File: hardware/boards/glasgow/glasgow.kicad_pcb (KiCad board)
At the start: 4 copper layers, 80 x 49 mm, 240 parts, among them J1 USB_B_Micro, J10 Conn_01x03, J2 Conn_02x10_Odd_Even, J3 Conn_02x10_Odd_Even, J4 Conn_01x02, J5 Conn_02x22_Odd_Even, J6 Conn_01x08, J7 Conn_01x08, J8 Conn_01x08, J9 Conn_01x08, U1 CY7C68013A-56LTX, U10 SN74LVC1T45DRL, U11 SN74LVC1T45DRL, U12 ADC081C021CIMM, U13 DAC081C081CIMK, U14 TPS73101DBV, U15 TPD3S014, U16 SN74LVC1T45DRL, U17 SN74LVC1T45DRL, U18 SN74LVC1T45DRL, U19 PCA6408APW, U2 CAT24M01W, U20 DAC081C081CIMK, U21 ADC081C021CIMM, U22 SN74LVC1T45DRL, U23 SN74LVC1T45DRL, U24 SN74LVC1T45DRL, U25 SN74LVC1T45DRL, U26 SN74LVC1T45DRL, U27 SN74LVC1T45DRL, U28 SN74LVC1T45DRL, U29 SN74LVC1T45DRL, U3 CAT24C256W, U30 ICE40HX8K-BG121, U31 TPS73101DBV, U32 SN74LVC1T45DRL, U33 MG2040, U34 ATECC508A, U35 MG2040, U36 TLV75533PDRVR, U4 SN74LVC1T45DRL, U5 PCA6408APW, U6 SN74LVC1T45DRL, U7 LM3880MF-1AF, U8 TLV73312PQDRVRQ1, U9 SN74LVC1T45DRL, Y1 24M

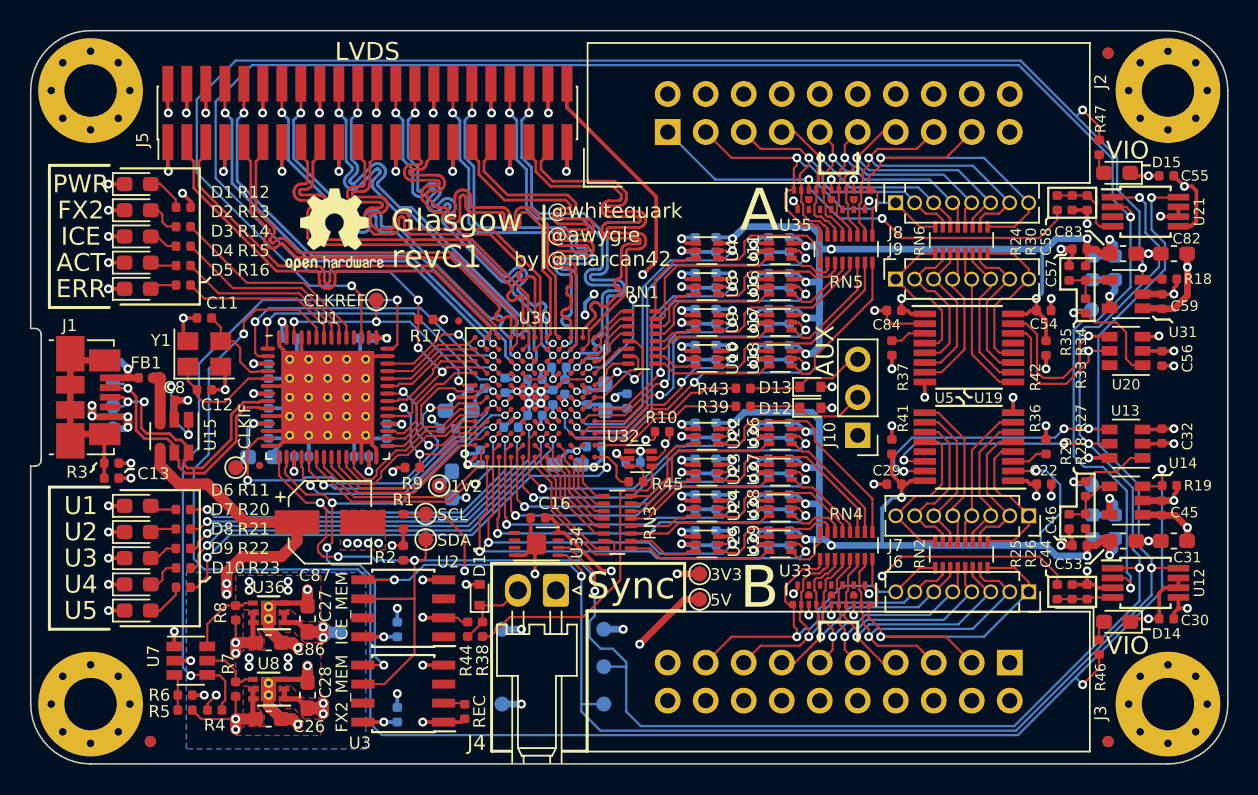
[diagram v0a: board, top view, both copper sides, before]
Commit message: revC1: 1BitSquared manufacturing changes.
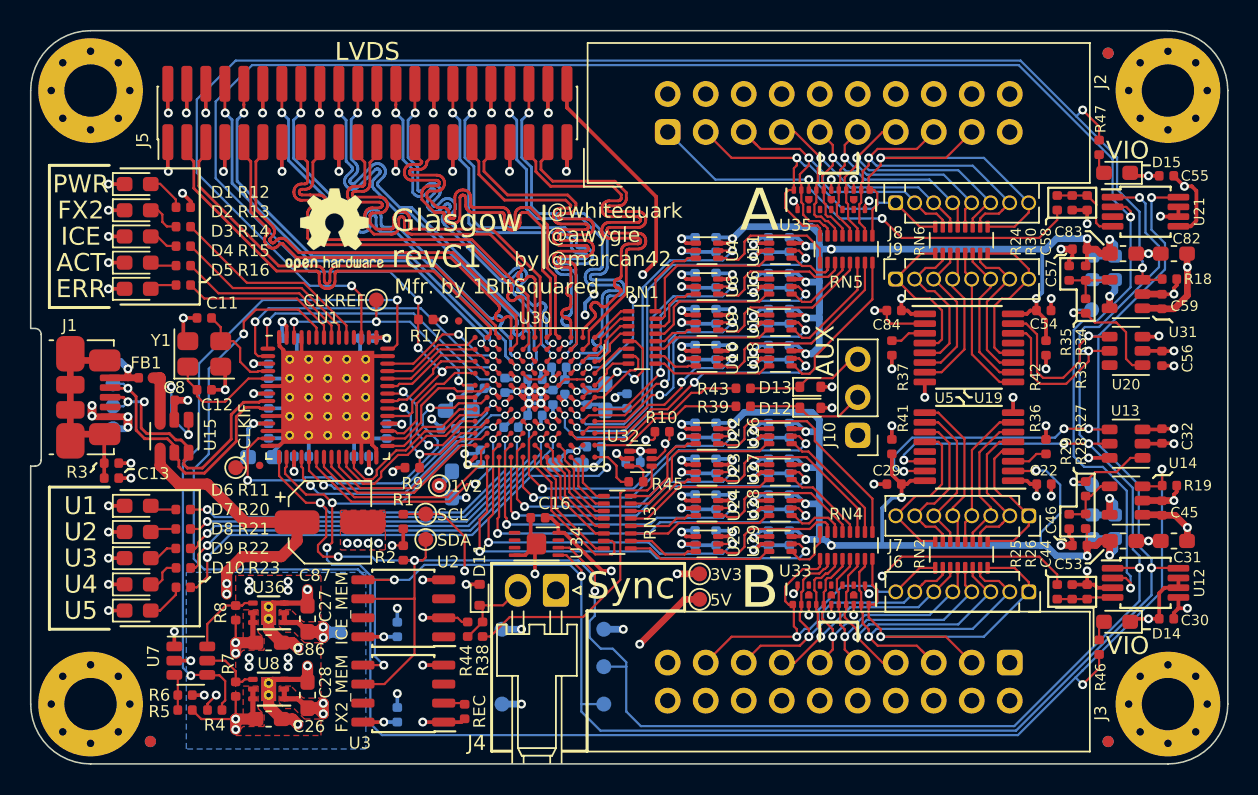
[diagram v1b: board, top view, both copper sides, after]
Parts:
- removed NONO_HANA: MECHOKKU, Glasgow:nono_hana
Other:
- board text added: "1BitSquared"
- board text added: "Manufactured by"
- board text added: "Mfr. by 1BitSquared"

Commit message: revC1: Brought Hannah back. :)
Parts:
- added NONO_HANA: MECHOKKU, Glasgow:nono_hana, B.Cu at (73.8, 82.5)
